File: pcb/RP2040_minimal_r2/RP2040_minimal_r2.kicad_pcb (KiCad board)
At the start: 2 copper layers, 52 x 51 mm, 34 parts, among them J1 USB_B_Micro, J2 Conn_01x02, J3 Conn_02x18_Odd_Even, J4 Conn_02x18_Odd_Even, U1 NCP1117-3.3_SOT223, U2 W25Q128JVS, U3 RP2040, Y1 ABM8-272-T3

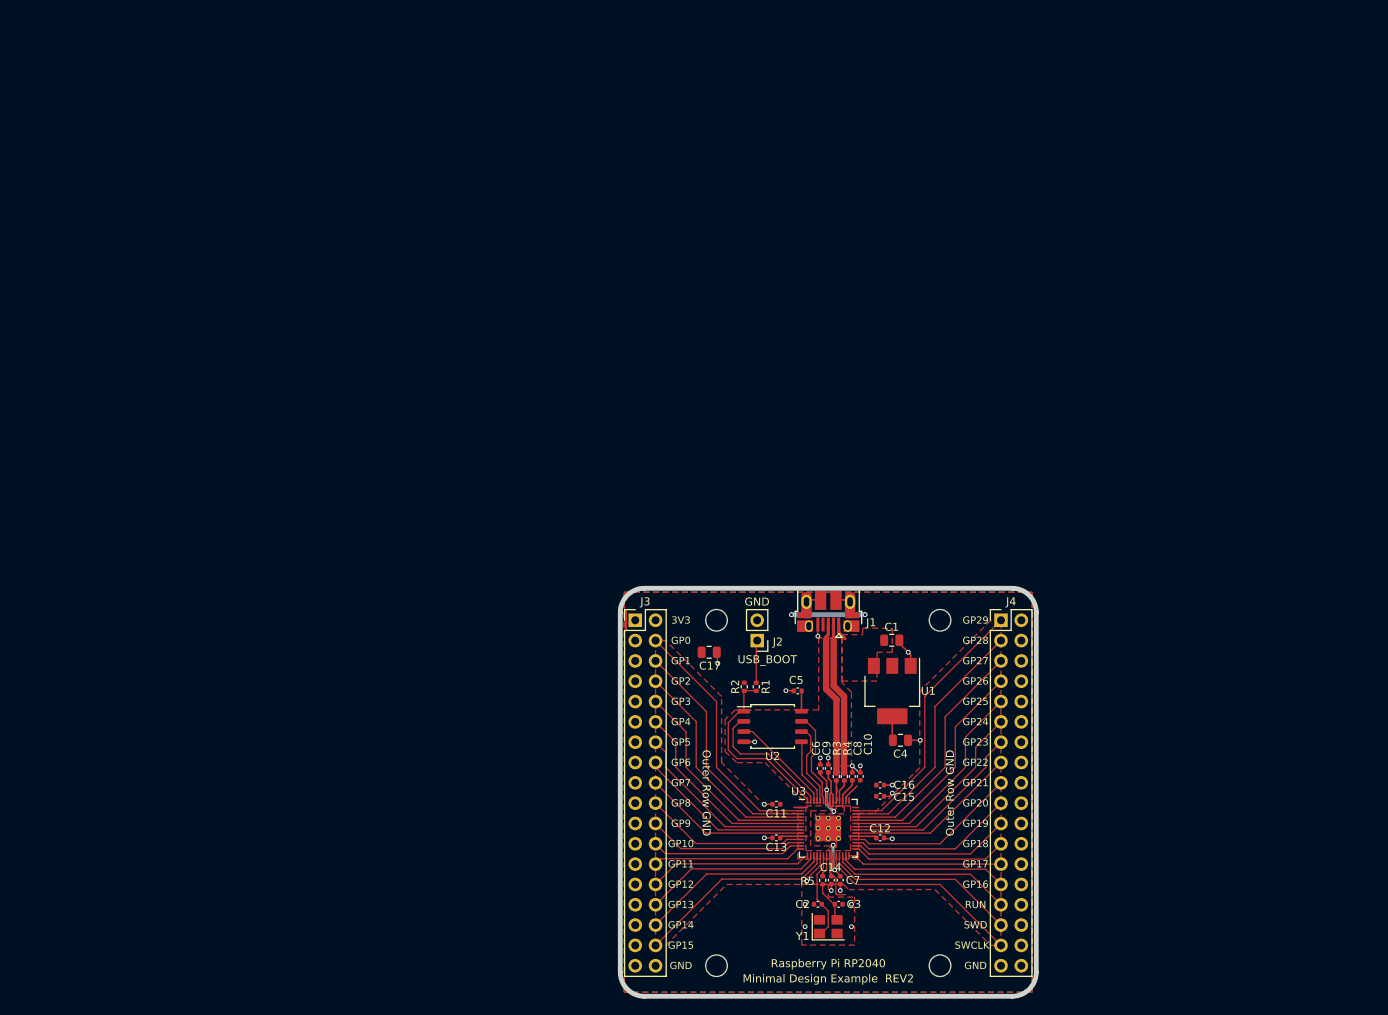
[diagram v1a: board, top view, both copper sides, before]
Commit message: add ddr contacts to pcb
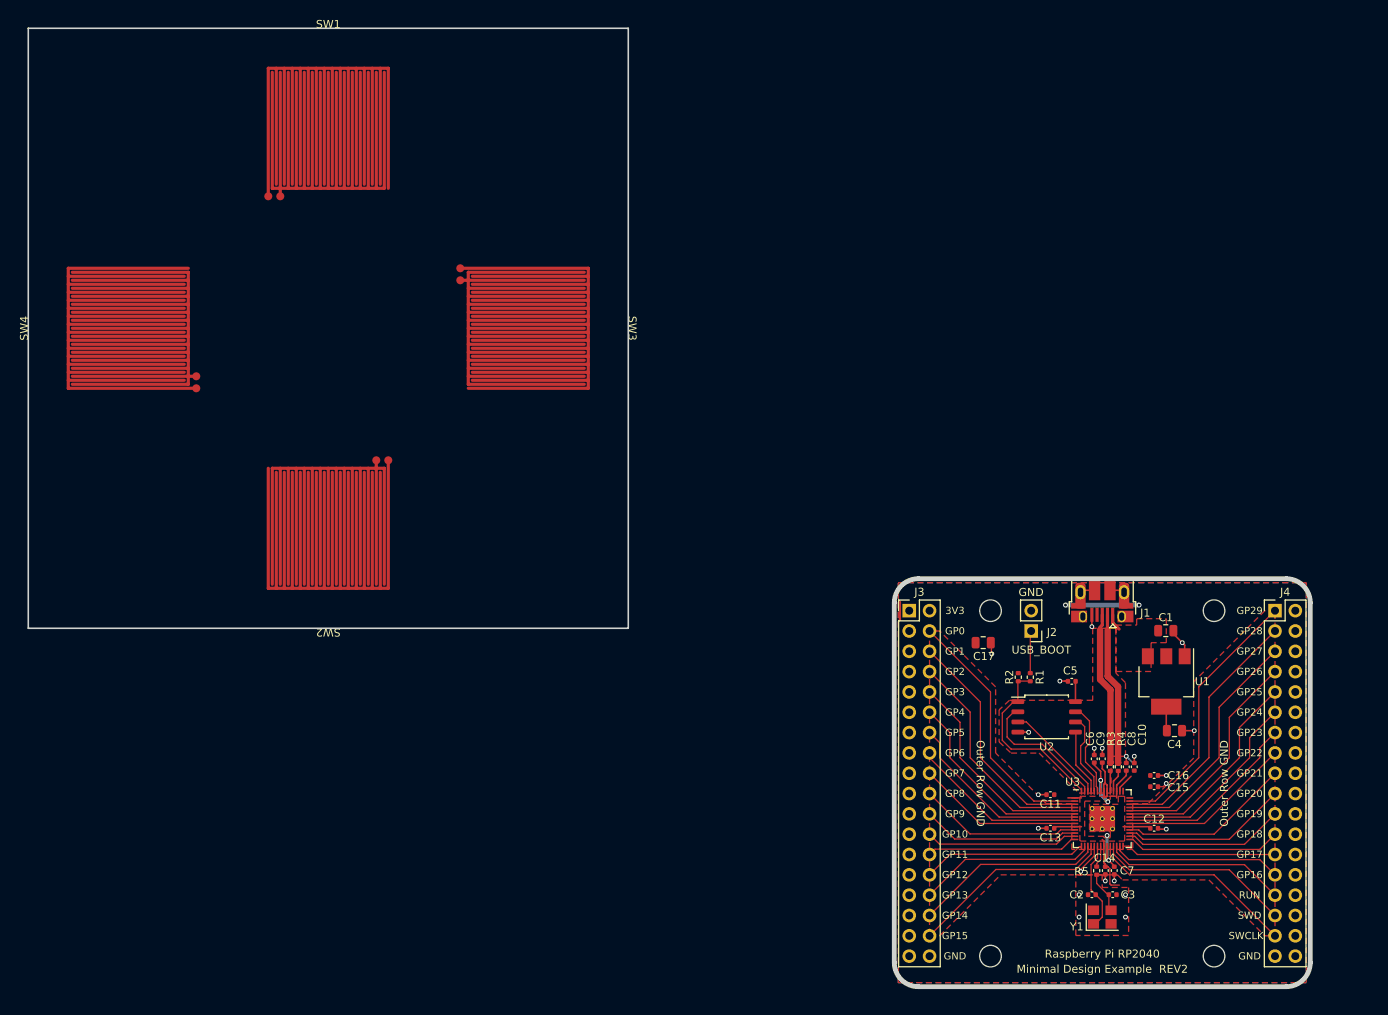
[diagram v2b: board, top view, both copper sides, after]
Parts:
- added SW1: DDR_North, Andrews_Library:DDR_CONTACT, F.Cu at (37.5, 12.5)
- added SW2: DDR_South, Andrews_Library:DDR_CONTACT, F.Cu at (37.5, 62.5)
- added SW3: DDR_East, Andrews_Library:DDR_CONTACT, F.Cu at (62.5, 37.5)
- added SW4: DDR_West, Andrews_Library:DDR_CONTACT, F.Cu at (12.5, 37.5)
- moved C12 34.3 mm to (140.7, 100.0)
- moved C15 34.3 mm to (140.7, 94.8)
- moved C16 34.3 mm to (140.7, 93.4)
- moved C3 34.3 mm to (135.6, 108.3)
- moved R5 34.3 mm to (133.6, 105.3)
- moved C1 34.3 mm to (142.2, 75.3)
- moved C10 34.3 mm to (138.2, 92.3)
- moved C11 34.3 mm to (127.8, 95.8)
- moved C13 34.3 mm to (127.8, 100.0)
- moved C14 34.3 mm to (134.6, 105.3)
- moved C17 34.3 mm to (119.4, 76.8)
- moved C4 34.3 mm to (143.3, 87.8)
- moved C5 34.3 mm to (130.4, 81.6)
- moved C6 34.3 mm to (133.2, 91.3)
- moved C7 34.3 mm to (135.8, 105.3)
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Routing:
- net +3V3: track 42.6 -> 40.3 mm
- net GND: track 29.7 -> 32.0 mm
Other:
- board size 52 x 51 mm -> 160.2 x 119.8 mm

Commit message: clean up pcb
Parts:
- removed H1, H2, H3, H4: MountingHole, MountingHole:MountingHole_2.7mm_M2.5
- removed J3, J4: Conn_02x18_Odd_Even, Connector_PinHeader_2.54mm:PinHeader_2x18_P2.54mm_Vertical
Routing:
- net /GPIO29_ADC3: track 33.2 -> 0.00 mm
- net /GPIO0: track 31.8 -> 0.00 mm
- net /GPIO28_ADC2: track 31.6 -> 0.00 mm
- net /GPIO1: track 30.2 -> 0.00 mm
- net /GPIO27_ADC1: track 29.9 -> 0.00 mm
- net /GPIO2: track 28.5 -> 0.00 mm
- net /GPIO26_ADC0: track 28.3 -> 0.00 mm
- net /GPIO3: track 26.9 -> 0.00 mm
- net /GPIO25: track 26.7 -> 0.00 mm
- net /SWCLK: track 25.9 -> 0.00 mm
- net /GPIO15: track 25.4 -> 0.00 mm
- net /GPIO4: track 25.3 -> 0.00 mm
- net /GPIO24: track 25.0 -> 0.00 mm
- net /SWD: track 24.3 -> 0.00 mm
- net /GPIO14: track 23.8 -> 0.00 mm
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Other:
- board text removed: "3V3"
- board text removed: "GP0"
- board text removed: "GP1"
- board text removed: "GP10"
- board text removed: "GP11"
- board text removed: "GP12"
- board text removed: "GP13"
- board text removed: "GP14"
- board text removed: "GP15"
- board text removed: "GP16"
- board text removed: "GP17"
- board text removed: "GP18"
- board text removed: "GP19"
- board text removed: "GP2"
- board text removed: "GP20"
- board text removed: "GP21"
- board text removed: "GP22"
- board text removed: "GP23"
- board text removed: "GP24"
- board text removed: "GP25"
- board text removed: "GP26"
- board text removed: "GP27"
- board text removed: "GP28"
- board text removed: "GP29"
- board text removed: "GP3"
- board text removed: "GP4"
- board text removed: "GP5"
- board text removed: "GP6"
- board text removed: "GP7"
- board text removed: "GP8"
- board text removed: "GP9"
- board text removed: "Minimal Design Example REV2"
- board text removed: "Outer Row GND"
- board text removed: "RUN"
- board text removed: "Raspberry Pi RP2040"
- board text removed: "SWCLK"
- board text removed: "SWD"

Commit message: add gnd zone
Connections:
- SW1 pad 2: unconnected-(SW1-Pad2) -> GND
- SW2 pad 2: unconnected-(SW2-Pad2) -> GND
- SW3 pad 2: unconnected-(SW3-Pad2) -> GND
- SW4 pad 2: unconnected-(SW4-Pad2) -> GND
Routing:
- net GND: vias 22 -> 26
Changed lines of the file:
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@@
 			(size 1 1)
 			(layers "F.Cu" "F.Mask" "F.Paste")
-			(net "unconnected-(SW3-Pad2)")
+			(net "GND")
 			(pinfunction "2_2")
 			(pintype "passive")
@@
 			(size 1 1)
 			(layers "F.Cu" "F.Mask" "F.Paste")
-			(net "unconnected-(SW4-Pad2)")
+			(net "GND")
 			(pinfunction "2_2")
 			(pintype "passive")
@@
 			(size 1 1)
 			(layers "F.Cu" "F.Mask" "F.Paste")
-			(net "unconnected-(SW2-Pad2)")
+			(net "GND")
 			(pinfunction "2_2")
 			(pintype "passive")
@@
 			(size 1 1)
 			(layers "F.Cu" "F.Mask" "F.Paste")
-			(net "unconnected-(SW1-Pad2)")
+			(net "GND")
 			(pinfunction "2_2")
 			(pintype "passive")
@@
 	)
 	(via
+		(at 54 30)
+		(size 0.6)
+		(drill 0.35)
+		(layers "F.Cu" "B.Cu")
+		(net "GND")
+	)
+	(via
 		(at 133.25 90.000008)
 		(size 0.6)
@@
 	)
 	(via
+		(at 21 45)
+		(size 0.6)
+		(drill 0.35)
+		(layers "F.Cu" "B.Cu")
+		(net "GND")
+	)
+	(via
 		(at 142.25 93.4)
 		(size 0.6)
@@
 	)
 	(via
+		(at 45 54)
+		(size 0.6)
+		(drill 0.35)
+		(layers "F.Cu" "B.Cu")
+		(net "GND")
+	)
+	(via
 		(at 128.95 81.6)
 		(size 0.6)
@@
 	)
 	(via
+		(at 30 21)
+		(size 0.6)
+		(drill 0.35)
+		(layers "F.Cu" "B.Cu")
+		(net "GND")
+	)
+	(via
 		(at 138.25 91)
 		(size 0.6)
@@
 			)
 		)
+	)
+	(zone
+		(net "GND")
+		(layer "B.Cu")
+		(hatch edge 0.508)
+		(connect_pads
+			(clearance 0.2)
+		)
+		(min_thickness 0.2)
+		(fill yes
+			(thermal_gap 0.3)
+			(thermal_bridge_width 0.3)
+			(island_removal_mode 0)
+		)
+		(polygon
+			(pts
+				(xy 75 75) (xy 0.085267 75) (xy -0.001057 0.001366) (xy 75 -0.084961)
+			)
+		)

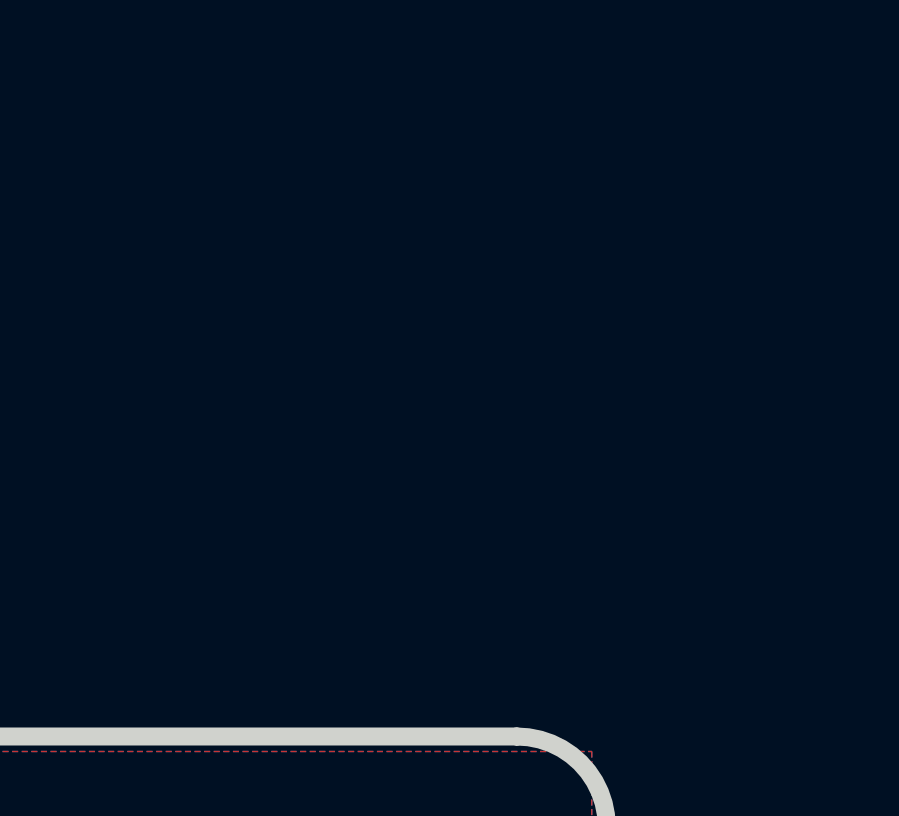
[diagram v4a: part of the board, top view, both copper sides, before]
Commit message: add usbc to schematic
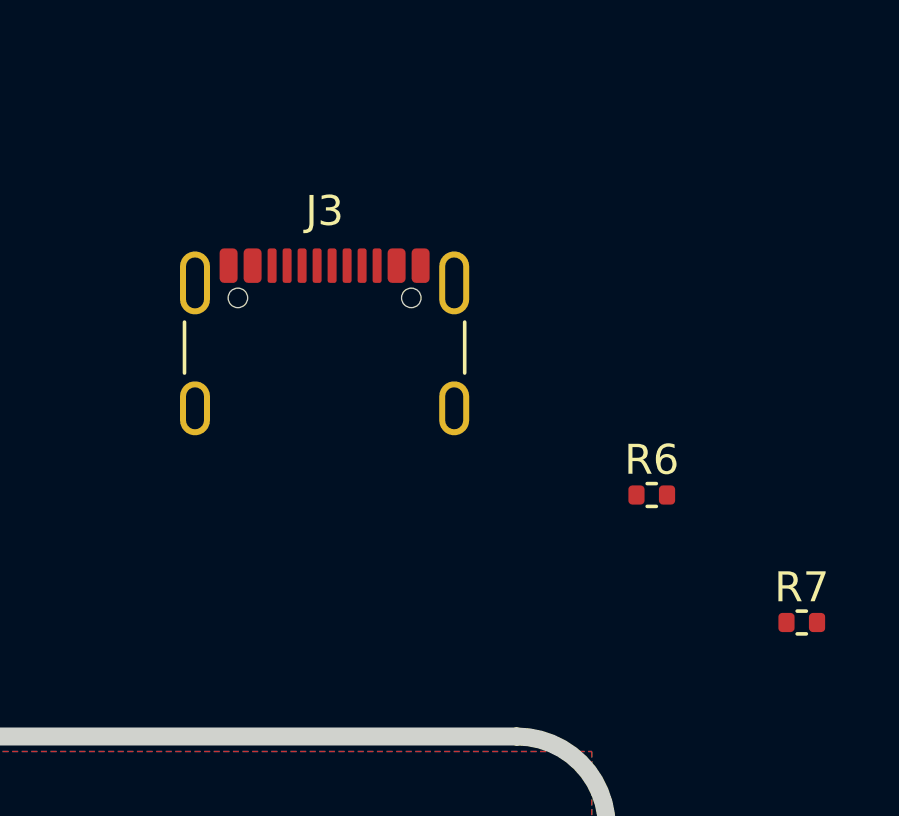
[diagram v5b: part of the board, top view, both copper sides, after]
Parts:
- added J3: USB_C_Receptacle, Connector_USB:USB_C_Receptacle_GCT_USB4105-xx-A_16P_TopMnt_Horizontal, F.Cu at (150.8, 56.8)
- added R6: 5.1k, Resistor_SMD:R_0402_1005Metric, F.Cu at (161.8, 60.8)
- added R7: 5.1k, Resistor_SMD:R_0402_1005Metric, F.Cu at (166.8, 65.0)

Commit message: working on pcb
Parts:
- removed J1: USB_B_Micro, RP2040_minimal:USB_Micro-B_Amphenol_10103594-0001LF_Horizontal_modified
- moved R7 165.2 mm to (10.8, 10.7), turned to -90 degrees
- moved R6 156.2 mm to (13.8, 10.8), turned to -90 degrees
- moved U1 148.9 mm to (6.75, 19.9)
- moved C1 148.9 mm to (6.69, 13.5)
- moved C4 148.9 mm to (7.78, 26.0)
- moved J3 147.8 mm to (12.5, 4.75), turned to 180 degrees
- moved C5 121.7 mm to (12.5, 51.7), turned to -90 degrees
- moved J2 120.6 mm to (6.24, 56.7), turned to -90 degrees
- moved R1 115.8 mm to (12.0, 56.9), turned to 180 degrees
- moved C17 114.8 mm to (16.2, 26.5)
- moved U2 114.7 mm to (17.0, 54.8), turned to 90 degrees
- moved C12 114.5 mm to (44.0, 38.7)
- moved C15 114.5 mm to (44.0, 33.5)
- moved C16 114.5 mm to (44.0, 32.1)
- moved C3 114.5 mm to (38.8, 47.0)
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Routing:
- net /QSPI_SD3: track 11.8 -> 40.2 mm
- net /QSPI_SCLK: track 10.4 -> 38.6 mm
- net /QSPI_SD0: track 8.20 -> 35.9 mm
- net /QSPI_SD1: track 16.8 -> 44.4 mm
- net /QSPI_SD2: track 12.9 -> 40.2 mm
- net /QSPI_SS: track 22.7 -> 49.3 mm
- net /USB_D-: track 19.1 -> 43.2 mm
- net /USB_D+: track 19.2 -> 40.0 mm
- net VBUS: track 2.11 -> 17.3 mm
- net +3V3: track 40.3 -> 33.0 mm, vias 2 -> 0
- net Net-(J3-CC1): track 0.00 -> 1.81 mm
- net Net-(J3-CC2): track 0.00 -> 1.80 mm
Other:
- board size 160.2 x 119.8 mm -> 75 x 75 mm

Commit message: finish pcb i think
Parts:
- SW1: footprint Andrews_Library:DDR_CONTACT -> Andrews_Library:DDR_CONTACT_MIRROR
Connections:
- SW1 pad 1: unconnected-(SW1-Pad1) -> /GPIO25
- SW2 pad 1: unconnected-(SW2-Pad1) -> /GPIO23
- SW3 pad 1: unconnected-(SW3-Pad1) -> /GPIO24
- SW4 pad 1: unconnected-(SW4-Pad1) -> /GPIO11
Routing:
- net /GPIO23: track 0.00 -> 23.3 mm
- net /GPIO25: track 0.00 -> 21.0 mm
- net /GPIO24: track 0.00 -> 15.5 mm
- net /GPIO11: track 0.00 -> 14.5 mm, vias 0 -> 2
- net GND: vias 26 -> 27

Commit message: move some stuff a bit
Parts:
- moved C17 13.9 mm to (21.4, 13.6)
- moved C5 5.79 mm to (14.2, 57.2)
- moved U2 5.79 mm to (18.6, 60.4)
- moved J2 5.79 mm to (7.90, 62.3)
- moved R1 5.79 mm to (13.7, 62.4)
- moved R2 5.79 mm to (13.7, 63.9)
- moved C4 0.75 mm to (7.78, 25.2)
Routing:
- net /QSPI_SD0: track 35.9 -> 43.5 mm
- net /QSPI_SCLK: track 38.6 -> 45.6 mm
- net /QSPI_SD3: track 40.2 -> 46.0 mm
- net /QSPI_SD2: track 40.2 -> 45.6 mm
- net /QSPI_SD1: track 44.4 -> 49.4 mm
- net /QSPI_SS: track 49.3 -> 54.1 mm
- net +3V3: track 33.0 -> 32.2 mm
